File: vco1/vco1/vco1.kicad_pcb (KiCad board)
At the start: 2 copper layers, 30 x 128.5 mm, 7 parts, among them U2 TL431DBZ

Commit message: Draw some more stuff
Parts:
- added C1: C, Capacitor_SMD:C_0603_1608Metric_Pad1.08x0.95mm_HandSolder, B.Cu at (67.9, 133.0)
- added C10: 10n, Capacitor_SMD:C_0603_1608Metric_Pad1.08x0.95mm_HandSolder, B.Cu at (67.1, 79.0)
- added C11: 100n, Capacitor_SMD:C_0603_1608Metric_Pad1.08x0.95mm_HandSolder, B.Cu at (98.9, 117.6)
- added C12: 100n, Capacitor_SMD:C_0603_1608Metric_Pad1.08x0.95mm_HandSolder, B.Cu at (98.9, 120.1)
- added C2: 10u or more, Capacitor_THT:CP_Radial_D5.0mm_P2.50mm, B.Cu at (71.5, 138.0)
- added C3: 10u or more, Capacitor_THT:CP_Radial_D5.0mm_P2.50mm, B.Cu at (70.5, 145.0)
- added C4: 100n X7R, Capacitor_SMD:C_0603_1608Metric_Pad1.08x0.95mm_HandSolder, B.Cu at (80.9, 104.0)
- added C5: 100n X7R, Capacitor_SMD:C_0603_1608Metric_Pad1.08x0.95mm_HandSolder, B.Cu at (82.9, 118.0)
- added C6: 3.9n C0G, Capacitor_SMD:C_0603_1608Metric_Pad1.08x0.95mm_HandSolder, B.Cu at (78.9, 119.0)
- added C7: 4.7u or so, Capacitor_SMD:C_0805_2012Metric_Pad1.18x1.45mm_HandSolder, B.Cu at (109.3, 100.6)
- added C8: 10n, Capacitor_SMD:C_0603_1608Metric_Pad1.08x0.95mm_HandSolder, B.Cu at (72.9, 116.0)
- added C9: 1u, Capacitor_SMD:C_0603_1608Metric_Pad1.08x0.95mm_HandSolder, B.Cu at (86.9, 85.0)
- added D1: LED sync, LED_SMD:LED_0603_1608Metric_Pad1.05x0.95mm_HandSolder, B.Cu at (70.4, 82.0)
- added D2: LED wave out, LED_SMD:LED_0603_1608Metric_Pad1.05x0.95mm_HandSolder, B.Cu at (108.9, 135.0)
- added FB1: FerriteBead_Small, Inductor_SMD:L_1206_3216Metric_Pad1.22x1.90mm_HandSolder, B.Cu at (61.3, 138.6)
- added FB2: FerriteBead_Small, Inductor_SMD:L_1206_3216Metric_Pad1.22x1.90mm_HandSolder, B.Cu at (61.3, 142.0)
- added FB3: FerriteBead_Small, Inductor_SMD:L_1206_3216Metric_Pad1.22x1.90mm_HandSolder, B.Cu at (61.3, 145.4)
- added J1: Conn_02x08_Odd_Even, Connector_IDC:IDC-Header_2x08_P2.54mm_Vertical, B.Cu at (98.6, 146.0)
- added J_CV1: AudioJack2_SwitchT, Connector_Audio:Jack_3.5mm_QingPu_WQP-PJ398SM_Vertical_CircularHoles, F.Cu at (80.0, 52.0)
- added J_CV2: AudioJack2_SwitchT, Connector_Audio:Jack_3.5mm_QingPu_WQP-PJ398SM_Vertical_CircularHoles, F.Cu at (100.0, 52.0)
- added J_FM1: AudioJack2_SwitchT, Connector_Audio:Jack_3.5mm_QingPu_WQP-PJ398SM_Vertical_CircularHoles, F.Cu at (90.0, 95.0)
- added J_PULSE1: AudioJack2_SwitchT, Connector_Audio:Jack_3.5mm_QingPu_WQP-PJ398SM_Vertical_CircularHoles, F.Cu at (90.0, 138.0)
- added J_PWM1: AudioJack2_SwitchT, Connector_Audio:Jack_3.5mm_QingPu_WQP-PJ398SM_Vertical_CircularHoles, F.Cu at (100.0, 95.0)
- added J_SAW1: AudioJack2_SwitchT, Connector_Audio:Jack_3.5mm_QingPu_WQP-PJ398SM_Vertical_CircularHoles, F.Cu at (80.0, 138.0)
- added J_SYNC1: AudioJack2_SwitchT, Connector_Audio:Jack_3.5mm_QingPu_WQP-PJ398SM_Vertical_CircularHoles, F.Cu at (80.0, 95.0)
- added J_TRI1: AudioJack2_SwitchT, Connector_Audio:Jack_3.5mm_QingPu_WQP-PJ398SM_Vertical_CircularHoles, F.Cu at (100.0, 138.0)
- added Q1: BC847, Package_TO_SOT_SMD:SOT-23, B.Cu at (68.8, 95.2)
- added R1: 10k, Resistor_SMD:R_0603_1608Metric_Pad0.98x0.95mm_HandSolder, B.Cu at (106.9, 123.0)
- added R10: 270, Resistor_SMD:R_0603_1608Metric_Pad0.98x0.95mm_HandSolder, B.Cu at (72.2, 106.3)
- added R11: 267k, Resistor_SMD:R_0603_1608Metric_Pad0.98x0.95mm_HandSolder, B.Cu at (72.6, 113.2)
- added R12: 4k3, Resistor_SMD:R_0603_1608Metric_Pad0.98x0.95mm_HandSolder, B.Cu at (74.3, 108.1)
- added R13: 22k1, Resistor_SMD:R_0603_1608Metric_Pad0.98x0.95mm_HandSolder, B.Cu at (66.6, 105.5)
- added R14: 49k9, Resistor_SMD:R_0603_1608Metric_Pad0.98x0.95mm_HandSolder, B.Cu at (80.3, 43.8)
- added R15: 49k9, Resistor_SMD:R_0603_1608Metric_Pad0.98x0.95mm_HandSolder, B.Cu at (97.4, 63.2)
- added R16: 1M maybe?, Resistor_SMD:R_0603_1608Metric_Pad0.98x0.95mm_HandSolder, B.Cu at (82.7, 77.3)
- added R17: 49k9, Resistor_SMD:R_0603_1608Metric_Pad0.98x0.95mm_HandSolder, B.Cu at (82.7, 63.1)
- added R18: 100k, Resistor_SMD:R_0603_1608Metric_Pad0.98x0.95mm_HandSolder, B.Cu at (96.6, 84.3)
- added R19: 100k, Resistor_SMD:R_0603_1608Metric_Pad0.98x0.95mm_HandSolder, B.Cu at (98.3, 82.3)
- added R2: 39k, Resistor_SMD:R_0603_1608Metric_Pad0.98x0.95mm_HandSolder, B.Cu at (108.9, 125.0)
- added R20: 499k, Resistor_SMD:R_0603_1608Metric_Pad0.98x0.95mm_HandSolder, B.Cu at (75.9, 111.0)
- added R21: 499k, Resistor_SMD:R_0603_1608Metric_Pad0.98x0.95mm_HandSolder, B.Cu at (86.1, 87.0)
- added R22: 10k, Resistor_SMD:R_0603_1608Metric_Pad0.98x0.95mm_HandSolder, B.Cu at (71.4, 79.0)
- added R23: 20k, Resistor_SMD:R_0603_1608Metric_Pad0.98x0.95mm_HandSolder, B.Cu at (62.9, 91.0)
- added R24: 47k5, Resistor_SMD:R_0603_1608Metric_Pad0.98x0.95mm_HandSolder, B.Cu at (64.9, 89.0)
- added R25: 3k3, Resistor_SMD:R_0603_1608Metric_Pad0.98x0.95mm_HandSolder, B.Cu at (66.9, 130.0)
- added R26: 1k maybe, Resistor_SMD:R_0603_1608Metric_Pad0.98x0.95mm_HandSolder, B.Cu at (107.9, 132.0)
- added R27: 1k maybe?, Resistor_SMD:R_0603_1608Metric_Pad0.98x0.95mm_HandSolder, B.Cu at (68.2, 76.0)
- added R3: 1k, Resistor_SMD:R_0603_1608Metric_Pad0.98x0.95mm_HandSolder, B.Cu at (79.9, 129.8)
- added R4: 39k, Resistor_SMD:R_0603_1608Metric_Pad0.98x0.95mm_HandSolder, B.Cu at (107.1, 119.2)
- added R5: 39k, Resistor_SMD:R_0603_1608Metric_Pad0.98x0.95mm_HandSolder, B.Cu at (111.7, 121.0)
- added R6: 10k, Resistor_SMD:R_0603_1608Metric_Pad0.98x0.95mm_HandSolder, B.Cu at (111.0, 117.1)
- added R7: 10k, Resistor_SMD:R_0603_1608Metric_Pad0.98x0.95mm_HandSolder, B.Cu at (106.1, 115.9)
- added R8: 1k, Resistor_SMD:R_0603_1608Metric_Pad0.98x0.95mm_HandSolder, B.Cu at (89.9, 129.7)
- added R9: 1k, Resistor_SMD:R_0603_1608Metric_Pad0.98x0.95mm_HandSolder, B.Cu at (99.9, 130.0)
- added RV_CALIB1: 5k 10 turn, Potentiometer_THT:Potentiometer_Bourns_3266Y_Vertical, B.Cu at (63.0, 109.0)
- added RV_CV2: 100k?, Potentiometer_THT:Potentiometer_Alpha_RD901F-40-00D_Single_Vertical_CircularHoles, F.Cu at (95.7, 66.5)
- added RV_PWM1: 100k, Potentiometer_THT:Potentiometer_Alpha_RD901F-40-00D_Single_Vertical_CircularHoles, F.Cu at (95.7, 80.5)
- added RV_RANGE1: 100k, Potentiometer_THT:Potentiometer_Alpha_RD901F-40-00D_Single_Vertical_CircularHoles, F.Cu at (79.7, 66.5)
- added RV_TUNE1: 100k, Potentiometer_THT:Potentiometer_Alpha_RD901F-40-00D_Single_Vertical_CircularHoles, F.Cu at (79.7, 80.5)
- added SW1: SW_SPDT, Button_Switch_THT:SW_Slide_SPDT_Straight_CK_OS102011MS2Q, B.Cu at (112.0, 99.5)
- added U1: SSI2131, Package_SO:STC_SOP-16_3.9x9.9mm_P1.27mm, B.Cu at (82.0, 111.0)
- added U3: TL074, Package_SO:SOIC-14_3.9x8.7mm_P1.27mm, B.Cu at (90.5, 120.5)
- U2: moved to B.Cu
- moved U2 85.5 mm to (71.1, 131.1), turned to 180 degrees
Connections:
- U2 pad 1: unconnected-(U2-K-Pad1) -> +2V5
- U2 pad 2: unconnected-(U2-REF-Pad2) -> +2V5
- U2 pad 3: unconnected-(U2-A-Pad3) -> GND

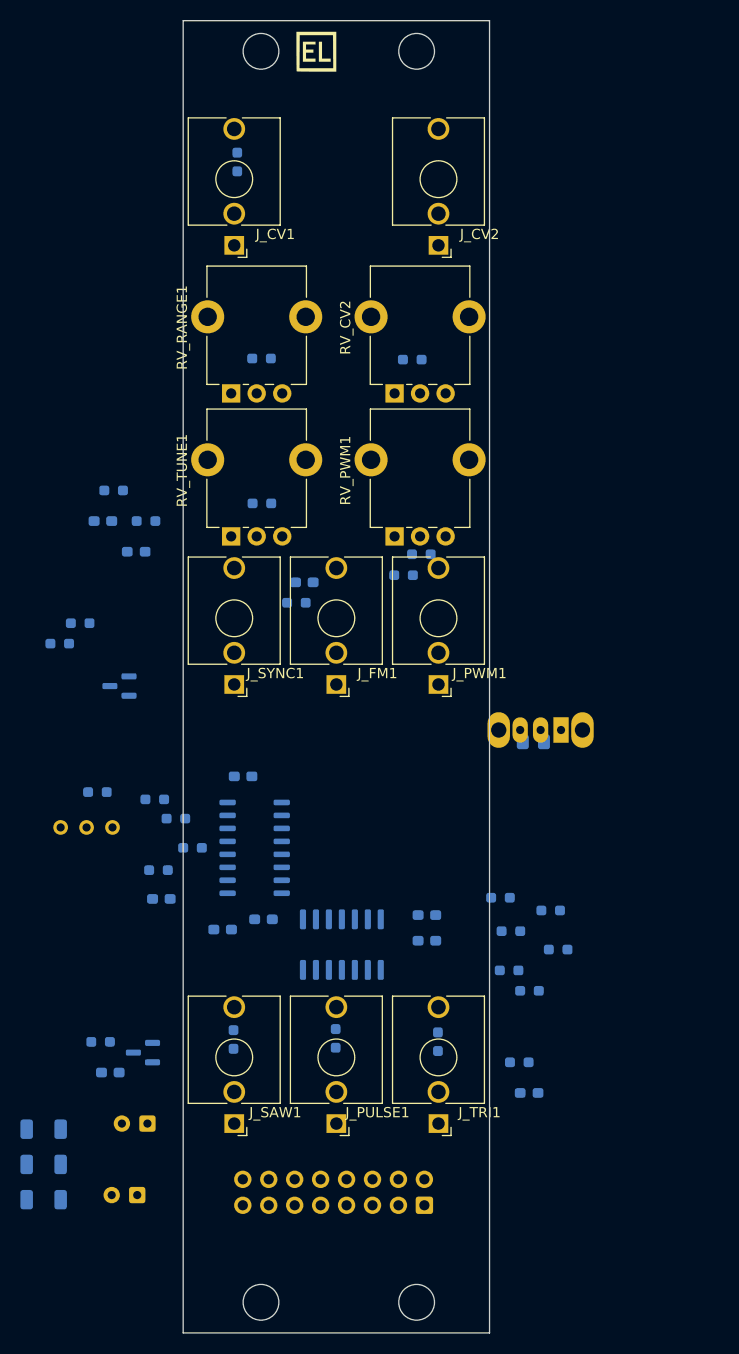
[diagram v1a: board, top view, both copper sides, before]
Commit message: Route most of the board
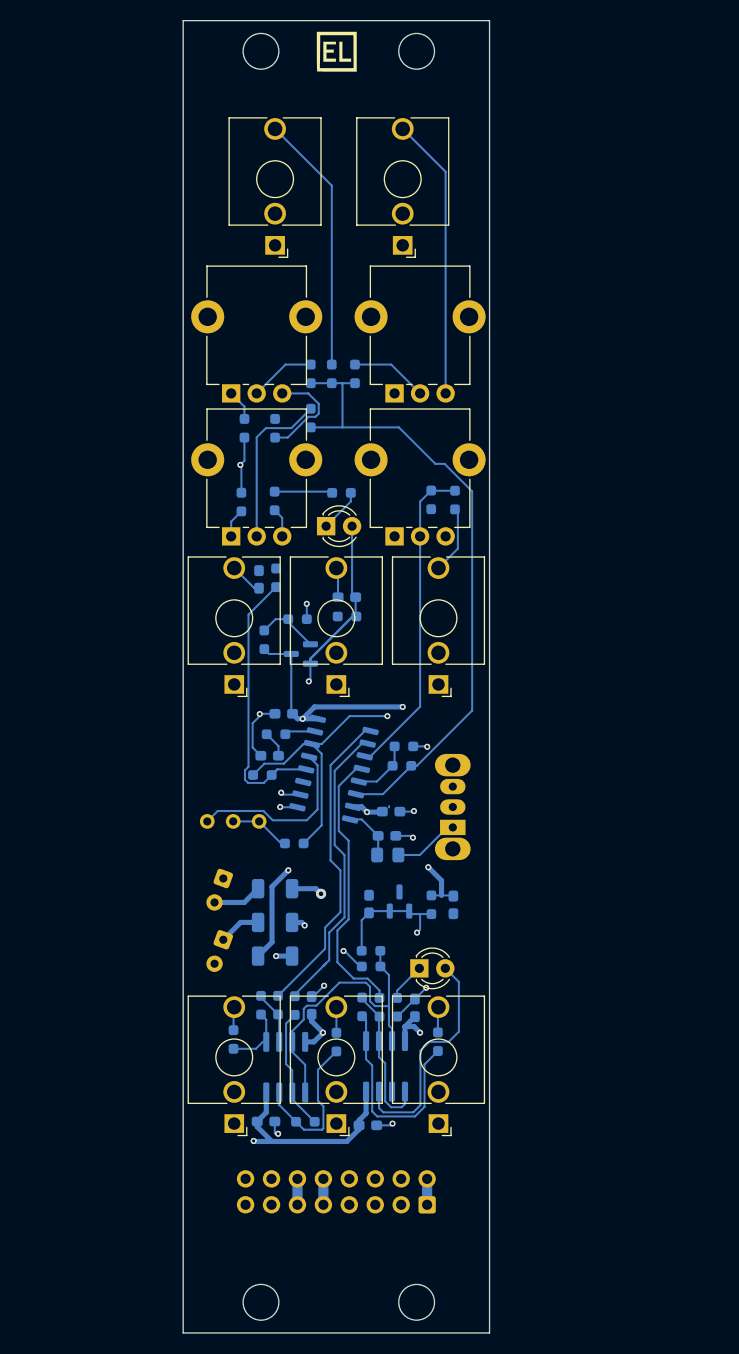
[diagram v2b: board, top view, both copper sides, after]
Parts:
- removed U3: TL074, Package_SO:SOIC-14_3.9x8.7mm_P1.27mm
- added C13: 100n, Capacitor_SMD:C_0603_1608Metric_Pad1.08x0.95mm_HandSolder, B.Cu at (101.5, 116.6)
- added C14: 100n, Capacitor_SMD:C_0603_1608Metric_Pad1.08x0.95mm_HandSolder, B.Cu at (83.1, 137.8)
- added C15: 100n, Capacitor_SMD:C_0603_1608Metric_Pad1.08x0.95mm_HandSolder, B.Cu at (87.6, 126.4)
- added R28: 0, Resistor_SMD:R_0603_1608Metric_Pad0.98x0.95mm_HandSolder, B.Cu at (84.0, 77.0)
- added R29: 0, Resistor_SMD:R_0603_1608Metric_Pad0.98x0.95mm_HandSolder, B.Cu at (80.7, 77.1)
- added R30: 0, Resistor_SMD:R_0603_1608Metric_Pad0.98x0.95mm_HandSolder, B.Cu at (84.0, 69.9)
- added R31: 0, Resistor_SMD:R_0603_1608Metric_Pad0.98x0.95mm_HandSolder, B.Cu at (81.0, 69.9)
- added R32: 20k, Resistor_SMD:R_0603_1608Metric_Pad0.98x0.95mm_HandSolder, B.Cu at (93.4, 121.1)
- added R33: 20k, Resistor_SMD:R_0603_1608Metric_Pad0.98x0.95mm_HandSolder, B.Cu at (93.4, 122.6)
- added U4: TL072, Package_SO:SOIC-8_3.9x4.9mm_P1.27mm, B.Cu at (85.0, 132.5)
- added U5: TL072, Package_SO:SOIC-8_3.9x4.9mm_P1.27mm, B.Cu at (94.8, 132.4)
- C1: value C -> 100n
- D1, D2: footprint LED_SMD:LED_0603_1608Metric_Pad1.05x0.95mm_HandSolder -> LED_THT:LED_D3.0mm; moved to F.Cu
- FB1, FB2, FB3: value FerriteBead_Small -> 0
- Q1: value BC847 -> DNP
- R13: value 22k1 -> 20k
- R23: value 20k -> DNP
- R24: value 47k5 -> DNP
- R25: value 3k3 -> 1k
- R26: value 1k maybe -> 1k
- R27: value 1k maybe? -> 1k
- RV_CALIB1: value 5k 10 turn -> 1010 turn
- U2: value TL431DBZ -> TL43BLI
- moved R25 35.1 mm to (99.3, 116.6), turned to 90 degrees
- moved FB3 32.9 mm to (84.0, 121.6)
- moved FB2 32.8 mm to (84.0, 118.3)
- moved FB1 32.7 mm to (84.0, 115.0)
- moved C3 32.1 mm to (78.9, 114.0), turned to -110 degrees
- moved C1 30.2 mm to (93.2, 116.5), turned to 90 degrees
- moved U2 29.2 mm to (96.2, 116.3), turned to 90 degrees
- moved R4 27.5 mm to (87.0, 137.8), turned to 0 degrees
- moved R6 26.7 mm to (85.9, 126.4), turned to 90 degrees
- moved R2 26.3 mm to (82.6, 126.4), turned to 90 degrees
- moved R11 25.9 mm to (96.4, 103.0), turned to 0 degrees
- moved C10 25.0 mm to (91.0, 86.5), turned to 0 degrees
- moved R12 23.4 mm to (96.6, 101.1), turned to 0 degrees
- moved R1 22.9 mm to (84.3, 126.4), turned to 90 degrees
- moved R14 22.7 mm to (89.6, 64.6)
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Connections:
- RV_RANGE1 pad 1: +12V -> Net-(R31-Pad1)
- RV_RANGE1 pad 3: GND -> Net-(R30-Pad2)
- RV_TUNE1 pad 1: +12V -> Net-(R29-Pad1)
- RV_TUNE1 pad 3: GND -> Net-(R28-Pad2)
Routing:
- net -12V: track 0.00 -> 101.1 mm, vias 0 -> 4
- net +12V: track 0.00 -> 100.8 mm, vias 0 -> 2
- net +2V5: track 0.00 -> 79.1 mm, vias 0 -> 2
- net +5V: track 0.00 -> 69.0 mm, vias 0 -> 4
- net /EXPO_FREQ: track 0.00 -> 63.3 mm
- net /HARD_SYNC: track 0.00 -> 37.9 mm, vias 0 -> 2
- net Net-(J1-Pin_1): track 0.00 -> 37.8 mm, vias 0 -> 1
- net /1.25V: track 0.00 -> 34.7 mm
- net Net-(J1-Pin_10): track 0.00 -> 33.1 mm, vias 0 -> 1
- net /PWM_CTRL: track 0.00 -> 31.4 mm
- net /SAW_OUT: track 0.00 -> 30.8 mm
- net GND: track 0.00 -> 29.3 mm, vias 0 -> 10
- net /PULSE_OUT: track 0.00 -> 29.2 mm
- net Net-(J1-Pin_11): track 0.00 -> 29.0 mm, vias 0 -> 1
- net Net-(J_CV2-PadT): track 0.00 -> 27.6 mm
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- added copper zone on In2.Cu, net GND
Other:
- copper layers 2 -> 4
- rule pad_to_mask_clearance: 0 -> 0.05
- board text added: "CV1"
- board text added: "CV2"
- board text added: "CV2 DEPTH"
- board text added: "FM"
- board text added: "OCTAVE"
- board text added: "PULSE"
- board text added: "PWM"
- board text added: "SAW"
- board text added: "SYNC"
- board text added: "TRIANGLE"
- board text added: "TUNE"

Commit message: More routing and stuff
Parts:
- removed FB1, FB2, FB3: 0, Inductor_SMD:L_1206_3216Metric_Pad1.22x1.90mm_HandSolder
- C2, C3: value 10u or more -> 10u
- C7: value 4.7u or so -> 2.2u
- C9: value 1u -> 2.2u; footprint Capacitor_SMD:C_0603_1608Metric_Pad1.08x0.95mm_HandSolder -> Capacitor_SMD:C_0805_2012Metric_Pad1.18x1.45mm_HandSolder
- RV_CALIB1: value 1010 turn -> 10k 3266Y-103
- RV_CV2: value 100k? -> 100k; footprint Potentiometer_THT:Potentiometer_Alpha_RD901F-40-00D_Single_Vertical_CircularHoles -> Pot:RV9012NO
- RV_PWM1, RV_RANGE1, RV_TUNE1: footprint Potentiometer_THT:Potentiometer_Alpha_RD901F-40-00D_Single_Vertical_CircularHoles -> Pot:RV9012NO
- U2: value TL43BLI -> TL431BCDBZR
- U4, U5: value TL072 -> TL072HxD
- moved RV_CALIB1 9.82 mm to (85.1, 114.5), turned to 107 degrees
- moved RV_CV2 7.84 mm to (98.0, 59.0)
- moved RV_PWM1 7.84 mm to (98.0, 73.0)
- moved RV_RANGE1 7.84 mm to (82.0, 59.0)
- moved RV_TUNE1 7.84 mm to (82.0, 73.0)
- moved R13 2.94 mm to (83.0, 111.1)
- moved C3 0.57 mm to (79.5, 114.0)
- moved R21 0.51 mm to (84.6, 84.6)
- moved D1 0.18 mm to (88.8, 79.5)
- moved C2 0.07 mm to (79.0, 120.0)
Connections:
- J1 pad 1: Net-(J1-Pin_1) -> -12V
- J1 pad 10: Net-(J1-Pin_10) -> +12V
- J1 pad 11: Net-(J1-Pin_11) -> +5V
- J1 pad 12: Net-(J1-Pin_11) -> +5V
- J1 pad 2: Net-(J1-Pin_1) -> -12V
- J1 pad 9: Net-(J1-Pin_10) -> +12V
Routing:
- net +12V: track 100.8 -> 144.5 mm, vias 2 -> 3
- net Net-(J1-Pin_1): track 37.8 -> 0.00 mm, vias 1 -> 0
- net Net-(J1-Pin_10): track 33.1 -> 0.00 mm, vias 1 -> 0
- net +5V: track 69.0 -> 98.4 mm, vias 4 -> 5
- net Net-(J1-Pin_11): track 29.0 -> 0.00 mm, vias 1 -> 0
- net -12V: track 101.1 -> 129.9 mm
- net GND: track 29.3 -> 47.8 mm, vias 10 -> 14
- net +2V5: track 79.1 -> 90.7 mm
- net Net-(R13-Pad2): track 5.96 -> 15.6 mm
- net Net-(U1-EXPO_SCALE): track 17.5 -> 14.0 mm
- net /LIN_FREQ: track 27.6 -> 30.9 mm
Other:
- board text added: "-12V"

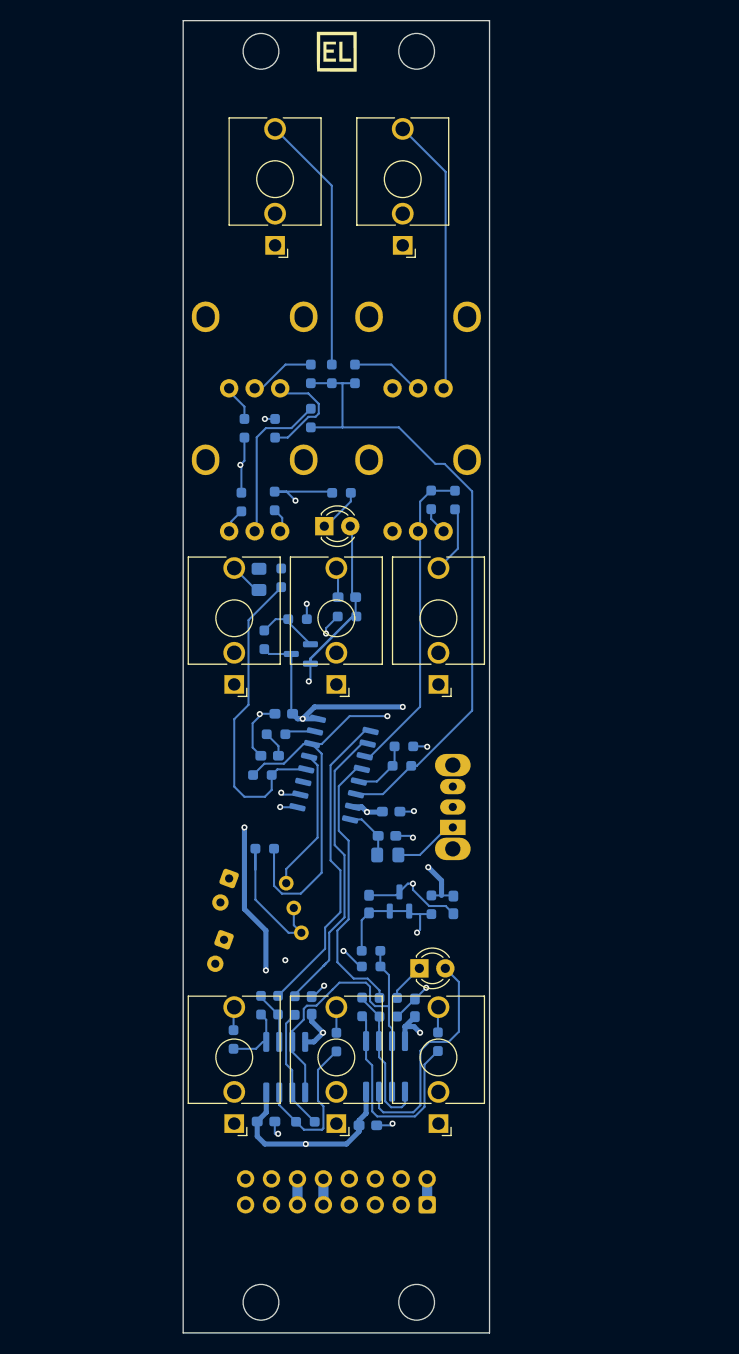
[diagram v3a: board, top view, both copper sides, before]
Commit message: Fix footprints, add test points
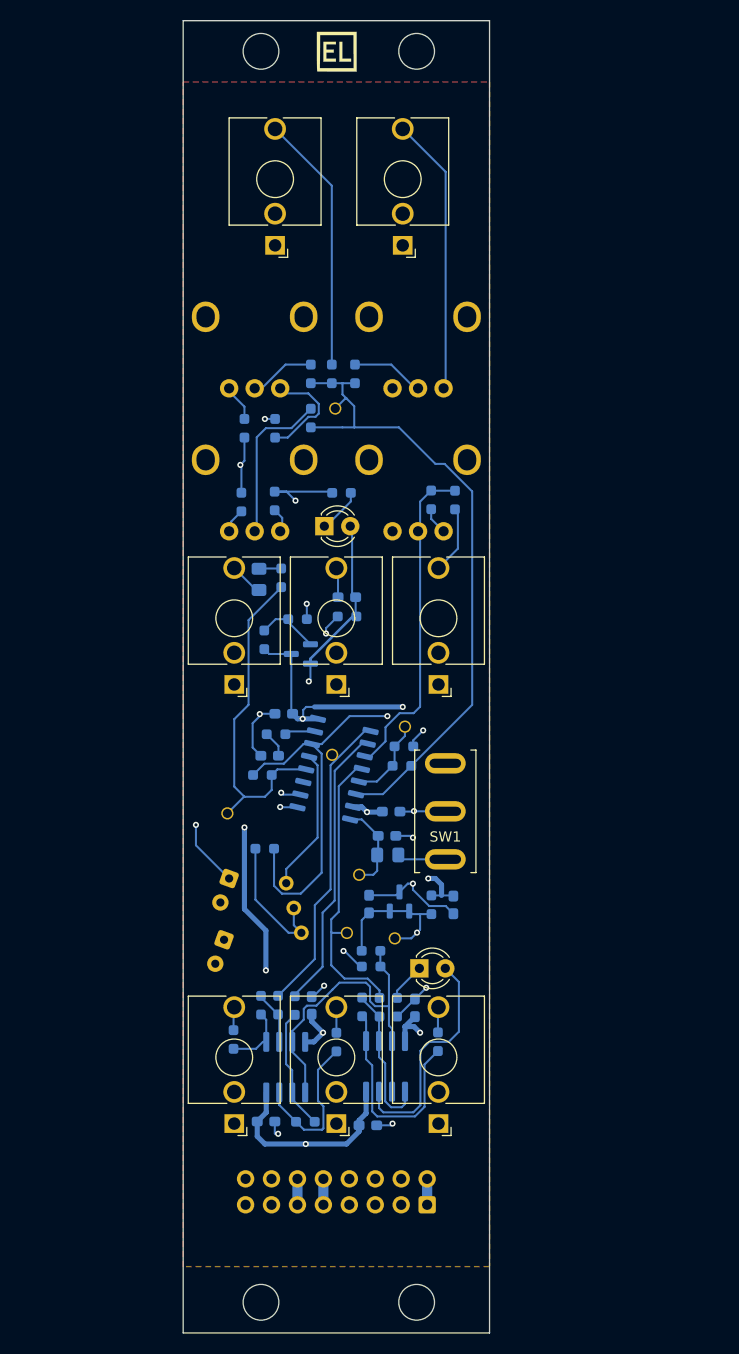
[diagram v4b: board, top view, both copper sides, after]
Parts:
- added TP1: TestPoint_Alt, Holes:TP_0.9mm, F.Cu at (91.0, 119.3)
- added TP2: TestPoint_Alt, Holes:TP_0.9mm, F.Cu at (89.9, 68.0)
- added TP3: TestPoint_Alt, Holes:TP_0.9mm, F.Cu at (95.7, 119.9)
- added TP4: TestPoint_Alt, Holes:TP_0.9mm, F.Cu at (79.3, 107.6)
- added TP5: TestPoint_Alt, Holes:TP_0.9mm, F.Cu at (96.7, 99.1)
- added TP6: TestPoint_Alt, Holes:TP_0.9mm, F.Cu at (92.2, 113.6)
- added TP7: TestPoint_Alt, Holes:TP_0.9mm, F.Cu at (89.6, 101.9)
- SW1: footprint Button_Switch_THT:SW_Slide_SPDT_Straight_CK_OS102011MS2Q -> Switch:SPDT big pads; moved to F.Cu
- moved REF** 10.1 mm to (78.6, 35.1)
- moved SW1 1.74 mm to (100.7, 107.4)
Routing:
- net GND: track 47.8 -> 58.1 mm, vias 14 -> 15
- net +5V: track 98.4 -> 103.5 mm
- net /TCAP: track 5.32 -> 8.80 mm
- net +2V5: track 90.7 -> 93.1 mm
- net /HF_TRACK: track 5.92 -> 8.27 mm
- net /LIN_FREQ: track 30.9 -> 33.2 mm
- net Net-(C9-Pad2): track 0.00 -> 2.29 mm
- net Net-(R13-Pad2): track 15.6 -> 13.6 mm
- net /TRI_OUT: track 27.1 -> 28.9 mm
- net Net-(SW1-A): track 6.45 -> 4.78 mm
- net /EXPO_FREQ: track 63.3 -> 64.9 mm
- net /PULSE_OUT: track 29.2 -> 28.0 mm
- net /PWM_CTRL: track 31.4 -> 32.2 mm
- net /SAW_OUT: track 30.8 -> 30.0 mm
- net +12V: vias 3 -> 2
- added copper zone on F.Cu, net GND
- added copper zone on In1.Cu, net GND
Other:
- board text added: "DJUP"
- board text added: "OKTAV"
- board text added: "OMFÅNG"
- board text added: "PULS"
- board text added: "SAKTA"
- board text added: "SNABB"
- board text added: "STÄM"
- board text added: "SYNK"
- board text added: "SÅGTAND"
- board text added: "TRIANGEL"
- board text added: "Tongenerator SSI2131"
- board text added: "VCO rev1 Elemental Instruments Jonas Norling 2026"
- board text added: "prototyp 1"
